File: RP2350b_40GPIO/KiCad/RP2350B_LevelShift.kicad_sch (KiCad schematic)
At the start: 59 parts, among them J1 +5V, J10 SPI, J13 USB_B_Micro, J2 Right GPIO, J3 VGA, J4 Left GPIO, J7 SWD, J9 BOOT SEL, U1 LD1117S33TR_SOT223, U11 74CBTD3861, U12 74CBTD3861, U13 74CBTD3861, U14 74CBTD3861, U2 W25Q16JVSSIQ, U5 RP2350B-QFN80, U7 TLV74311PDBVR, Y1 12MHz

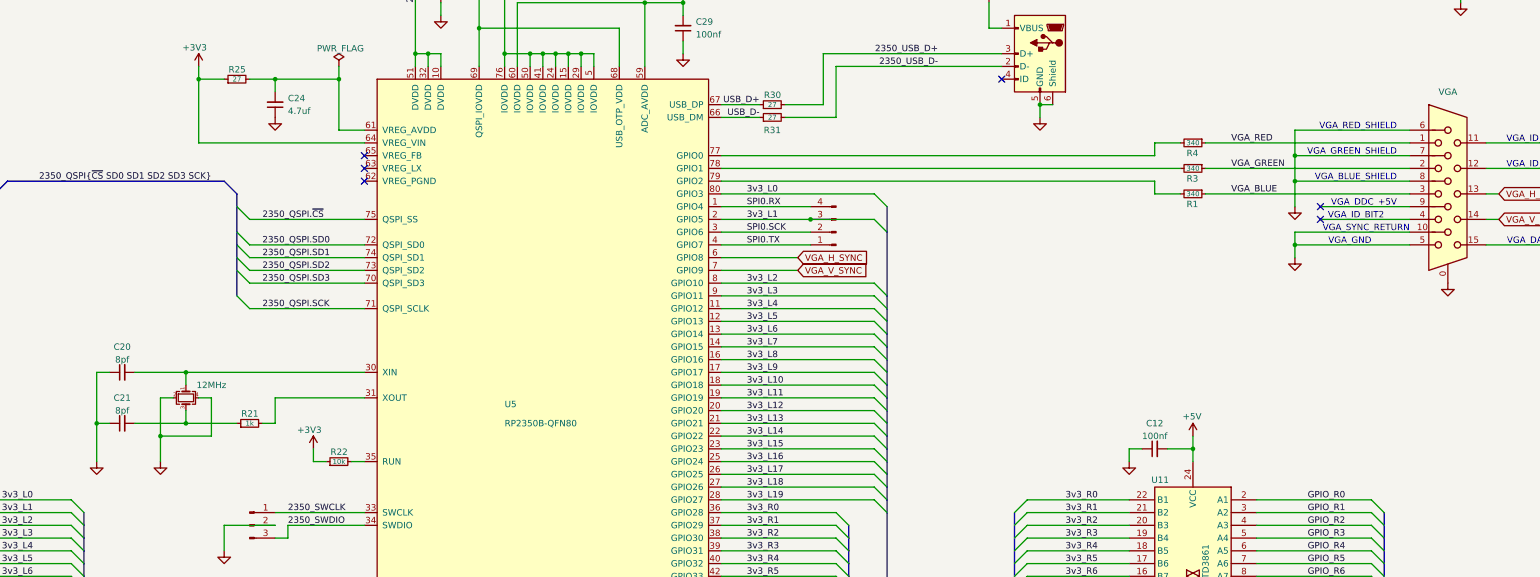
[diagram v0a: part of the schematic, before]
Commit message: - Updated To KiCad 10.0
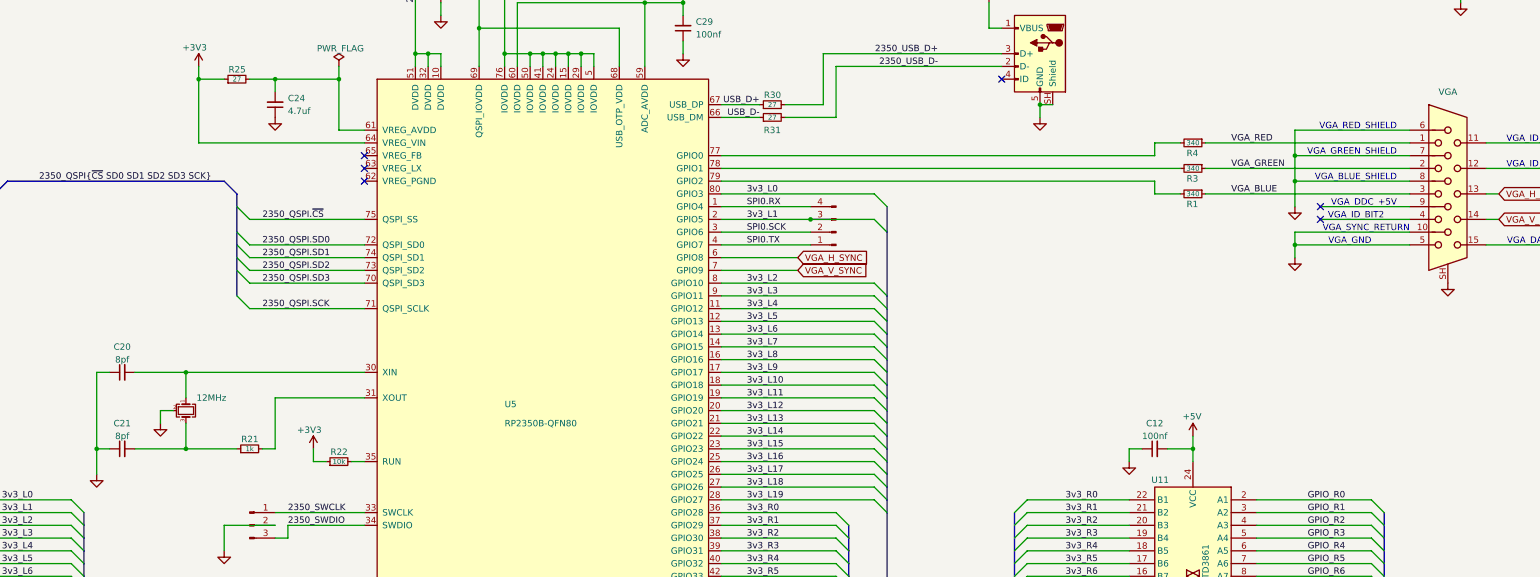
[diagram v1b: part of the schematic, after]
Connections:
- net GND: now also J13.SH (Shield), J3.SH; no longer J13.6 (Shield), J3.0
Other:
- moved on the sheet: C21, R21

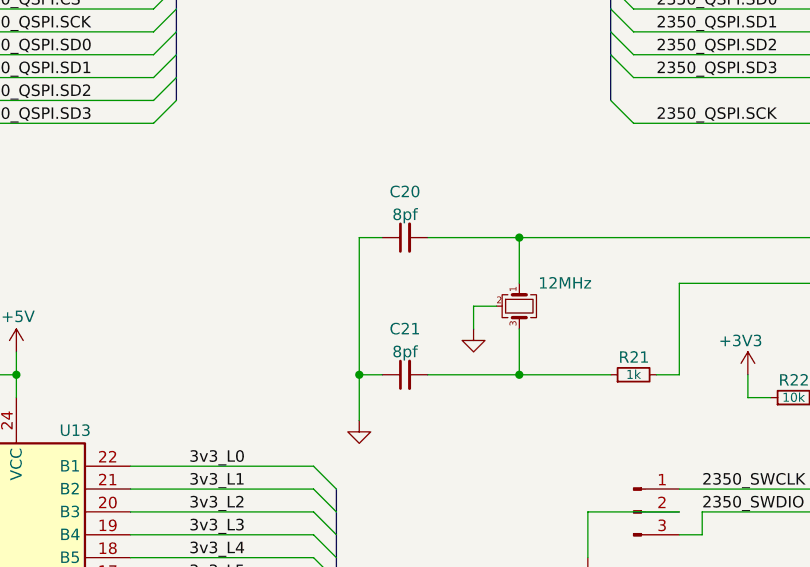
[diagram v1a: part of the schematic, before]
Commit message: - Updated Crystal Load Capacitance Value, 10pf may still be a bit low.
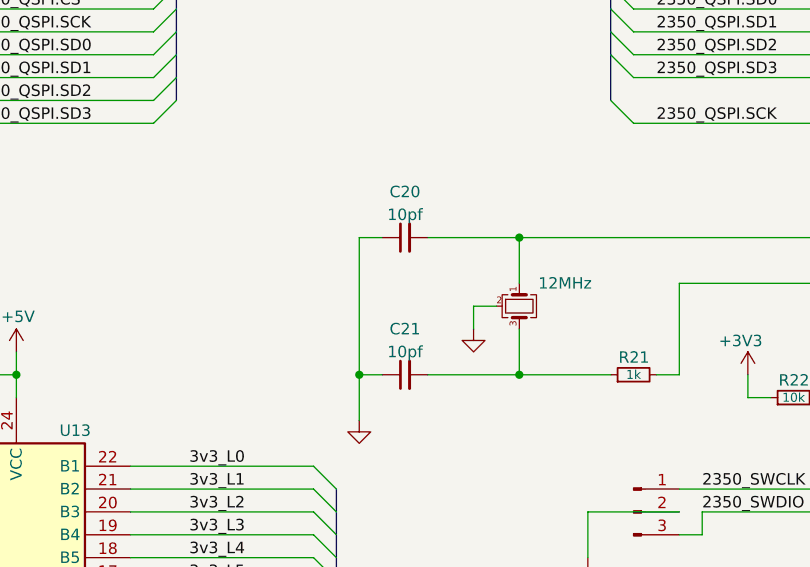
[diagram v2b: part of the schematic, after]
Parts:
- C20, C21: value 8pf -> 10pf
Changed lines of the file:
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@@
 			)
 		)
-		(property "Value" "8pf"
+		(property "Value" "10pf"
 			(at 187.96 195.58 90)
 			(show_name no)
@@
 			)
 		)
-		(property "Value" "8pf"
+		(property "Value" "10pf"
 			(at 187.96 210.82 90)
 			(show_name no)
